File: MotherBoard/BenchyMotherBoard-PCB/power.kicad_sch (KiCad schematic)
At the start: 153 parts, among them J1 PWR-CONN, U1 STM32MP157FAB1, U10 USB7206C, U2 TPS65400RGZT, U3 NCP51200, U4 ATTINY416-MNR, U5 MAX15027, U6 MAX15027, U7 SN74LVC1G32, U8 74HCT2G08, U9 AP2127K-3.3

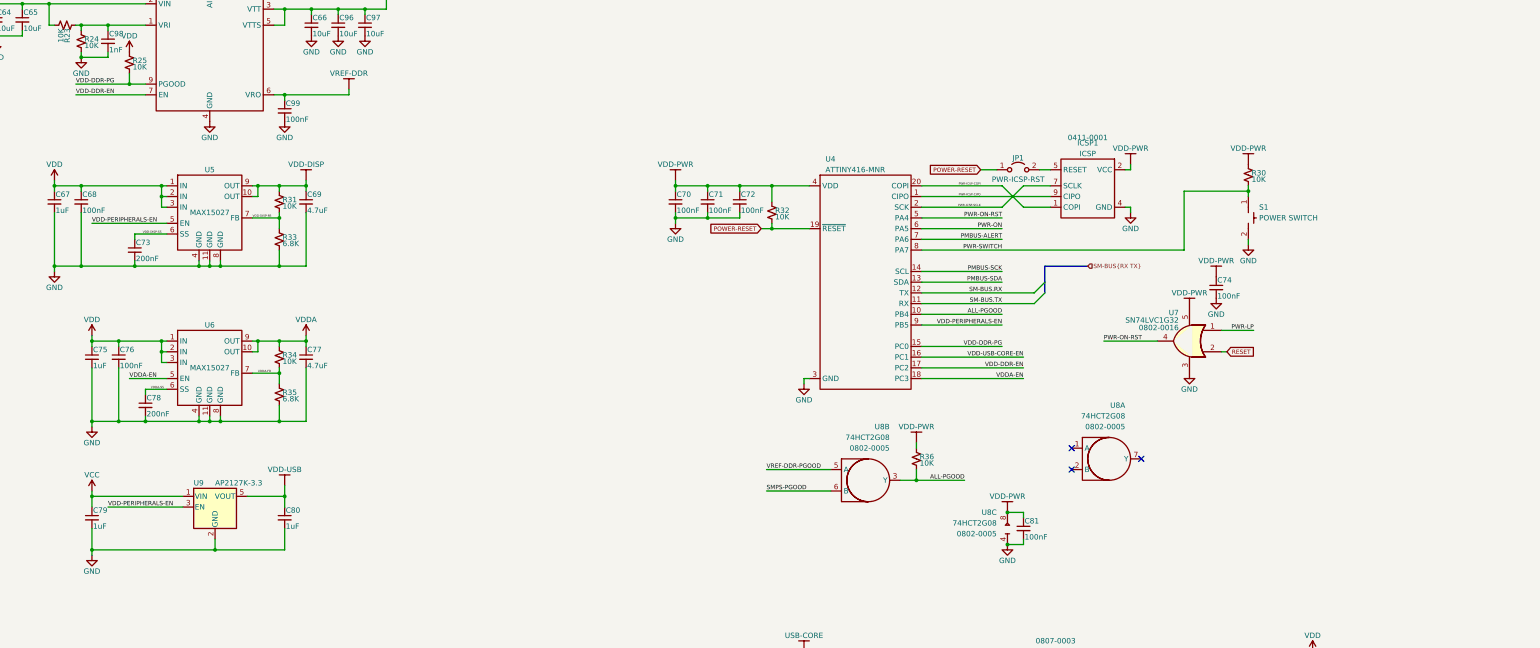
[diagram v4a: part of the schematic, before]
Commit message: Add PGOOD led and replace PWR switch
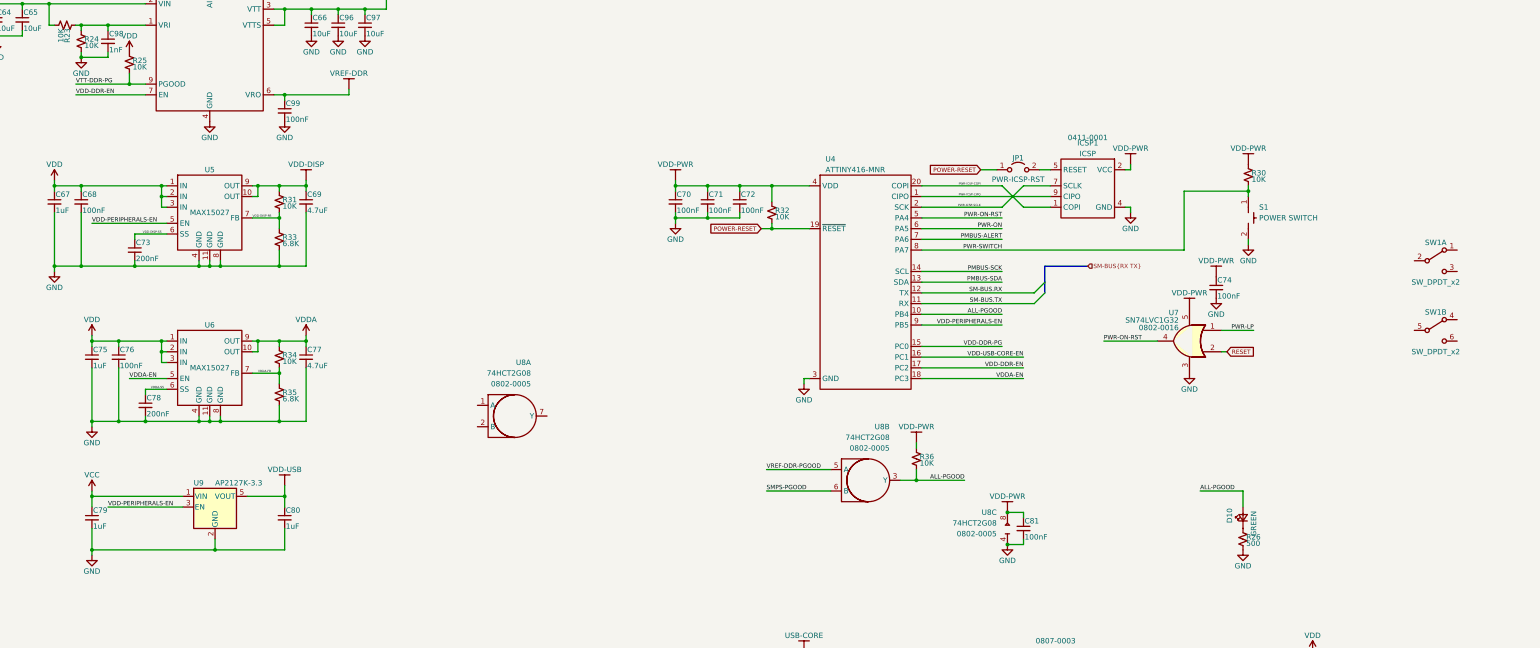
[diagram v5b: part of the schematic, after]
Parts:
- added D10: GREEN, LED_SMD:LED_0805_2012Metric, symbol Device:LED_Small
- added R26: 500, Resistor_SMD:R_0603_1608Metric, symbol Device:R_Small_US
- added SW1: SW_DPDT_x2, Daxxn_Switches:PHAP4383V, symbol Switch:SW_DPDT_x2
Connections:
- net ALL-PGOOD: now also D10.2 (A)
- net GND: now also R26.2
- net VDD-DDR-PG: no longer R25.2, U3.9 (PGOOD)
- new net: D10.1 (K), R26.1
- new net VTT-DDR-PG: R25.2, U3.9 (PGOOD)
- no-connect marks 3 -> 0
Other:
- moved on the sheet: U8A
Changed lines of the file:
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@@
   (junction (at 72.39 38.1) (diameter 0) (color 0 0 0 0)
   )
-  (no_connect (at 323.85 267.97))
-  (no_connect (at 307.34 270.51))
-  (no_connect (at 307.34 265.43))
   (bus_entry (at 298.45 231.14) (size 2.54 -2.54)
     (stroke (width 0) (type default) (color 0 0 0 0))
@@
     (stroke (width 0) (type default) (color 0 0 0 0))
   )
+  (wire (pts (xy 337.82 275.59) (xy 347.98 275.59))
+    (stroke (width 0) (type default) (color 0 0 0 0))
+  )
   (wire (pts (xy 90.17 128.27) (xy 90.17 129.54))
     (stroke (width 0) (type default) (color 0 0 0 0))
@@
     (stroke (width 0) (type default) (color 0 0 0 0))
   )
+  (wire (pts (xy 347.98 279.4) (xy 347.98 275.59))
+    (stroke (width 0) (type default) (color 0 0 0 0))
+  )
   (wire (pts (xy 129.54 74.93) (xy 130.81 74.93))
     (stroke (width 0) (type default) (color 0 0 0 0))
@@
     (effects (font (size 1.016 1.016)) (justify left bottom))
   )
+  (label "ALL-PGOOD" (at 337.82 275.59 0)
+    (effects (font (size 1.016 1.016)) (justify left bottom))
+  )
   (label "VDDA-EN" (at 83.82 248.92 0)
     (effects (font (size 1.016 1.016)) (justify left bottom))
@@
     (effects (font (size 0.5 0.5)) (justify left bottom))
   )
-  (label "VDD-DDR-PG" (at 71.12 179.07 0)
+  (label "VTT-DDR-PG" (at 71.12 179.07 0)
     (effects (font (size 1.016 1.016)) (justify left bottom))
   )
@@
     (pin "1")
   )
+  (symbol (lib_id "Switch:SW_DPDT_x2") (at 393.7 220.98 0) (unit 1)
+    (in_bom yes) (on_board yes)
+    (property "Reference" "SW1" (id 0) (at 393.7 216.662 0))
+    (property "Value" "SW_DPDT_x2" (id 1) (at 393.7 226.06 0))
+    (property "Footprint" "Daxxn_Switches:PHAP4383V" (id 2) (at 393.7 220.98 0)
+      (effects (font (size 1.27 1.27)) hide)
+    )
+    (property "Datasheet" "https://www.mouser.com/datasheet/2/26/appm_s_a0001220312_1-2262200.pdf" (id 3) (at 393.7 220.98 0)
+      (effects (font (size 1.27 1.27)) hide)
+    )
+    (pin "1")
+    (pin "2")
+    (pin "3")
+    (pin "4")
+    (pin "5")
+    (pin "6")
+  )
   (symbol (lib_id "Daxxn_Power:VDD-CORE") (at 264.16 82.55 0) (unit 1)
     (in_bom no) (on_board no)
@@
     (pin "1")
   )
+  (symbol (lib_id "Device:R_Small_US") (at 347.98 287.02 0) (unit 1)
+    (in_bom yes) (on_board yes)
+    (property "Reference" "R26" (id 0) (at 348.742 286.512 0)
+      (effects (font (size 1.27 1.27)) (justify left))
+    )
+    (property "Value" "500" (id 1) (at 348.742 288.036 0)
+      (effects (font (size 1.27 1.27)) (justify left))
+    )
+    (property "Footprint" "Resistor_SMD:R_0603_1608Metric" (id 2) (at 347.98 287.02 0)
+      (effects (font (size 1.27 1.27)) hide)
+    )
+    (property "Datasheet" "~" (id 3) (at 347.98 287.02 0)
+      (effects (font (size 1.27 1.27)) hide)
+    )
+    (pin "1")
+    (pin "2")
+  )
   (symbol (lib_id "Device:R_Small_US") (at 119.38 252.73 0) (unit 1)
     (in_bom yes) (on_board yes)
@@
     (pin "1")
   )
+  (symbol (lib_id "Device:LED_Small") (at 347.98 281.94 90) (unit 1)
+    (in_bom yes) (on_board yes)
+    (property "Reference" "D10" (id 0) (at 344.805 283.21 0)
+      (effects (font (size 1.27 1.27)) (justify left))
+    )
+    (property "Value" "GREEN" (id 1) (at 350.52 286.385 0)
+      (effects (font (size 1.27 1.27)) (justify left))
+    )
+    (property "Footprint" "LED_SMD:LED_0805_2012Metric" (id 2) (at 347.98 281.94 90)
+      (effects (font (size 1.27 1.27)) hide)
+    )
+    (property "Datasheet" "~" (id 3) (at 347.98 281.94 90)
+      (effects (font (size 1.27 1.27)) hide)
+    )
+    (pin "1")
+    (pin "2")
+  )
   (symbol (lib_id "Device:C_Small") (at 72.39 207.01 0) (unit 1)
     (in_bom yes) (on_board yes)
@@
     (pin "2")
   )
+  (symbol (lib_id "Switch:SW_DPDT_x2") (at 393.7 237.49 0) (unit 2)
+    (in_bom yes) (on_board yes)
+    (property "Reference" "SW1" (id 0) (at 393.7 233.172 0))
+    (property "Value" "SW_DPDT_x2" (id 1) (at 393.7 242.57 0))
+    (property "Footprint" "Daxxn_Switches:PHAP4383V" (id 2) (at 393.7 237.49 0)
+      (effects (font (size 1.27 1.27)) hide)
+    )
+    (property "Datasheet" "~" (id 3) (at 393.7 237.49 0)
+      (effects (font (size 1.27 1.27)) hide)
+    )
+    (pin "1")
+    (pin "2")
+    (pin "3")
+    (pin "4")
+    (pin "5")
+    (pin "6")
+  )
   (symbol (lib_id "power:GND") (at 74.93 260.35 0) (unit 1)
     (in_bom yes) (on_board yes)
@@
     (pin "2")
   )
-  (symbol (lib_id "Daxxn_Logic:74HCT2G08") (at 314.96 267.97 0) (unit 1)
+  (symbol (lib_id "Daxxn_Logic:74HCT2G08") (at 173.99 257.81 0) (unit 1)
     (in_bom yes) (on_board yes)
-    (property "Reference" "U8" (id 0) (at 320.04 255.27 0)
+    (property "Reference" "U8" (id 0) (at 179.07 245.11 0)
       (effects (font (size 1.27 1.27)) (justify right))
     )
-    (property "Value" "74HCT2G08" (id 1) (at 320.04 257.81 0)
+    (property "Value" "74HCT2G08" (id 1) (at 179.07 247.65 0)
       (effects (font (size 1.27 1.27)) (justify right))
     )
-    (property "Footprint" "Package_SO:TSSOP-8_3x3mm_P0.65mm" (id 2) (at 314.96 247.65 0)
+    (property "Footprint" "Package_SO:TSSOP-8_3x3mm_P0.65mm" (id 2) (at 173.99 237.49 0)
       (effects (font (size 1.27 1.27)) hide)
     )
-    (property "Datasheet" "%LOCAL_DATASHEETS%\\74HC2G08.pdf" (id 3) (at 314.96 245.11 0)
+    (property "Datasheet" "%LOCAL_DATASHEETS%\\74HC2G08.pdf" (id 3) (at 173.99 234.95 0)
       (effects (font (size 1.27 1.27)) hide)
     )
-    (property "PartNumber" "0802-0005" (id 4) (at 320.04 260.35 0)
+    (property "PartNumber" "0802-0005" (id 4) (at 179.07 250.19 0)
       (effects (font (size 1.27 1.27)) (justify right))
     )
@@
     (pin "2")
   )
+  (symbol (lib_id "power:GND") (at 347.98 289.56 0) (unit 1)
+    (in_bom yes) (on_board yes)
+    (property "Reference" "#PWR0218" (id 0) (at 347.98 295.91 0)
+      (effects (font (size 1.27 1.27)) hide)
+    )
+    (property "Value" "GND" (id 1) (at 347.98 293.37 0))
+    (property "Footprint" "" (id 2) (at 347.98 289.56 0)
+      (effects (font (size 1.27 1.27)) hide)
+    )
+    (property "Datasheet" "" (id 3) (at 347.98 289.56 0)
+      (effects (font (size 1.27 1.27)) hide)
+    )
+    (pin "1")
+  )
   (symbol (lib_id "Device:C_Small") (at 300.99 34.29 0) (unit 1)

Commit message: Start DDR3 layout
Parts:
- removed R36: 10K, Resistor_SMD:R_0402_1005Metric, symbol Device:R_Small_US
- removed S1: POWER SWITCH, Daxxn_Switches:TL3365AF180QG, symbol Daxxn_Buttons:GENERIC-SWITCH-2P
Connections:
- net GND: now also SW1.3 (C)
- net PWR-SWITCH: now also SW1.2 (B)
- no-connect marks 0 -> 1
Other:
- note removed: "COMP NOT CALCULATED YET"
- moved on the sheet: R30, SW1A, SW1B, U8A

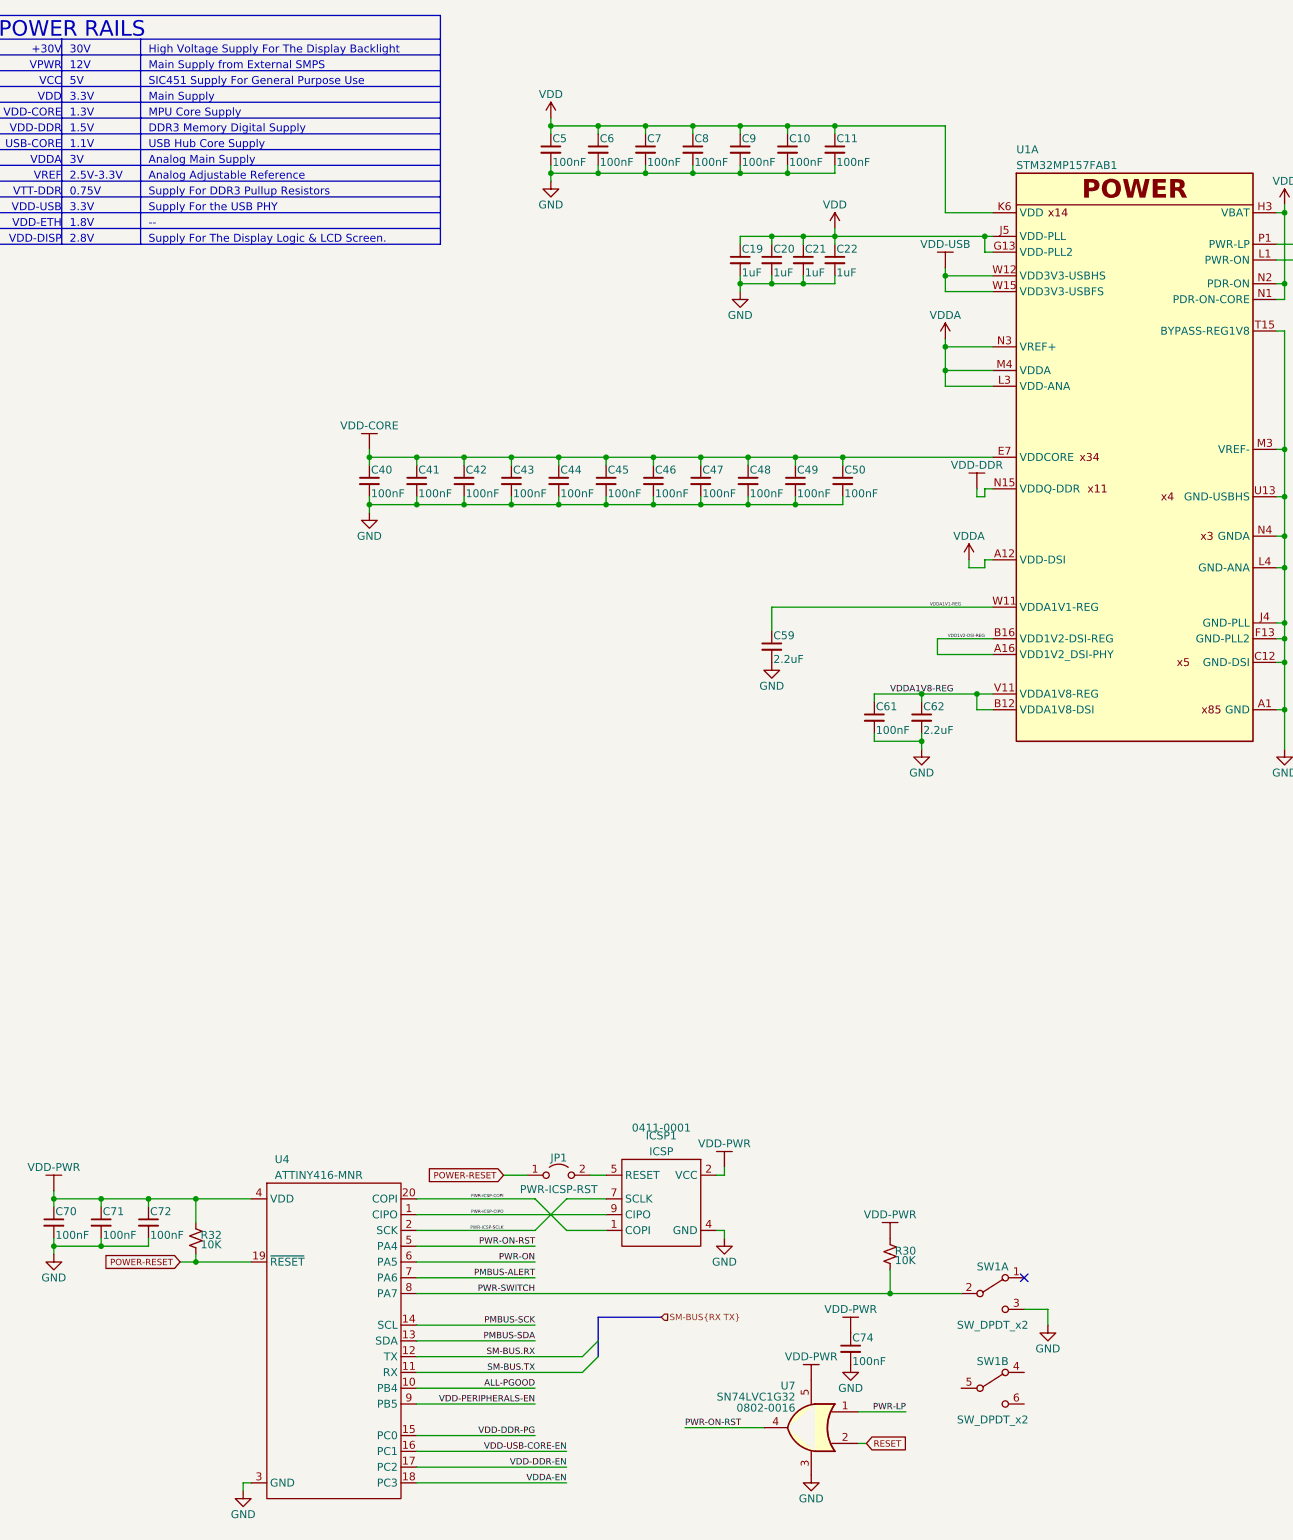
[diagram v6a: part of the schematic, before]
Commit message: Finish DDR3 memory layout
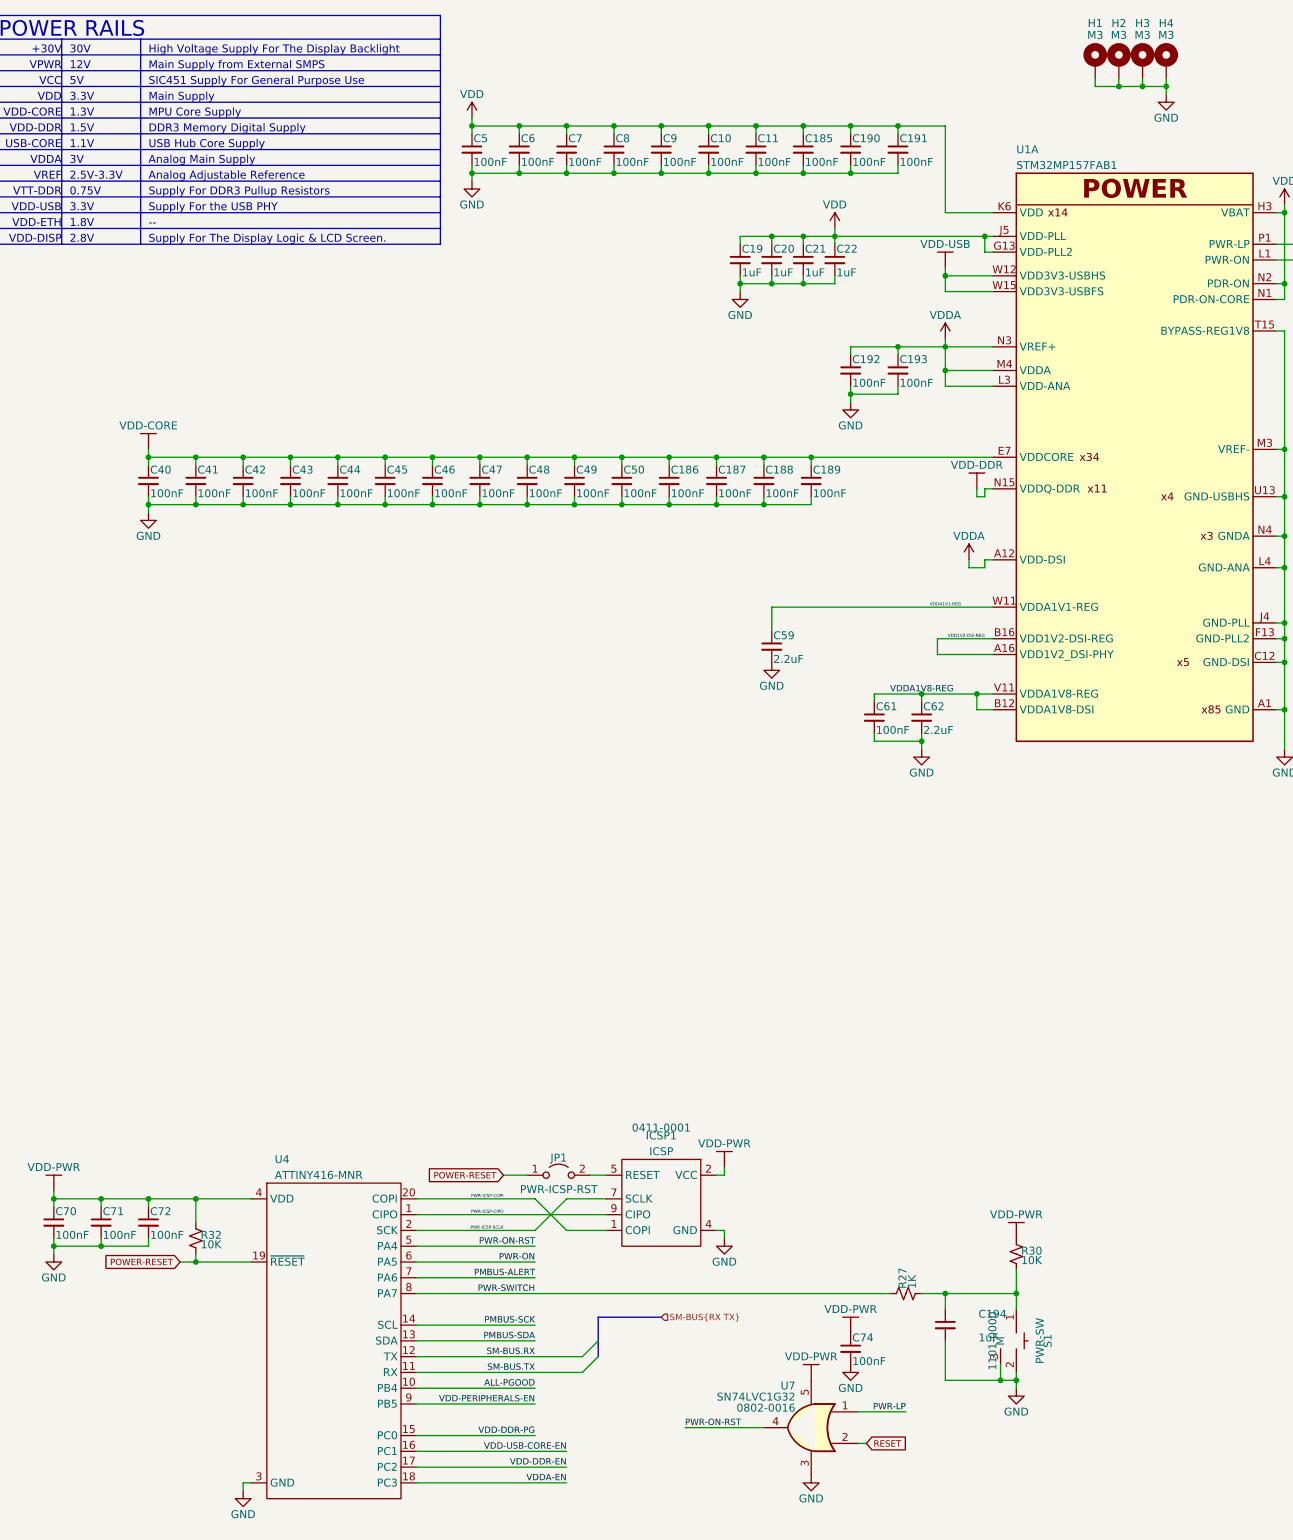
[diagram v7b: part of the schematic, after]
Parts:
- removed SW1: SW_DPDT_x2, Daxxn_Switches:PHAP4383V, symbol Switch:SW_DPDT_x2
- added C185, C186, C187, C188, C189, C190, C191, C192, C193: 100nF, Capacitor_SMD:C_0402_1005Metric, symbol Device:C_Small
- added C194: 1uF, Capacitor_SMD:C_0603_1608Metric, symbol Device:C_Small
- added H1, H2, H3, H4: M3, MountingHole:MountingHole_3.5mm_Pad_Via, symbol Mechanical:MountingHole_Pad
- added R27: 1K, Resistor_SMD:R_0402_1005Metric, symbol Device:R_Small_US
- added S1: PWR-SW, Daxxn_Switches:TL1105SF, symbol Daxxn_Buttons:GENERIC-SWITCH-2P-M
- U3: footprint Package_DFN_QFN:DFN-10-1EP_3x3mm_P0.5mm_EP1.7x2.5mm -> Daxxn_Packages:DFN-10-1EP_3x3mm_P0.5mm_EP1.65x2.38mm
- U4: footprint Package_DFN_QFN:VQFN-20-1EP_3x3mm_P0.4mm_EP1.7x1.7mm -> Daxxn_Packages:QFN-20-1EP_3x3mm_P0.4mm_EP1.65x1.65mm
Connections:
- net GND: now also C185.2, C186.2, C187.2, C188.2, C189.2, C190.2, C191.2, C192.2, C193.2, C194.2, H1.1, H2.1, H3.1, H4.1, S1.2, S1.3 (M)
- net PWR-SWITCH: now also R27.1; no longer R30.2
- net VDD: now also C185.1, C190.1, C191.1
- net VDD-CORE: now also C186.1, C187.1, C188.1, C189.1
- net VDDA: now also C192.1, C193.1
- new net: C194.1, R27.2, R30.2, S1.1
- no-connect marks 1 -> 0
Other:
- moved on the sheet: C10, C11, C40, C41, C42, C43, C44, C45, C46, C47, C48, C49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

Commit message: Mostly routed USB
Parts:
- removed C69: 4.7uF, Capacitor_SMD:C_0603_1608Metric, symbol Device:C_Small
- removed C70: 100nF, Capacitor_SMD:C_0402_1005Metric, symbol Device:C_Small
- removed C73: 200nF, Capacitor_SMD:C_0402_1005Metric, symbol Device:C_Small
- removed R31: 10K, Resistor_SMD:R_0402_1005Metric, symbol Device:R_Small_US
- removed R33: 6.8K, Resistor_SMD:R_0402_1005Metric, symbol Device:R_Small_US
- removed U5: MAX15027, Package_DFN_QFN:DFN-10-1EP_3x3mm_P0.5mm_EP1.65x2.38mm, symbol Daxxn_Regulators:MAX15027
- added H5, H6, H7, H8, H9: M2, MountingHole:MountingHole_2.2mm_M2_ISO7380_Pad, symbol Mechanical:MountingHole_Pad
- C67: value 1uF -> 100nF; footprint Capacitor_SMD:C_0603_1608Metric -> Capacitor_SMD:C_0402_1005Metric
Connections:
- net GND: now also H5.1, H6.1, H7.1, H8.1, H9.1
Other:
- note removed: "--"
- note removed: "1.8V"
- note removed: "2.8V"
- note removed: "Supply For The Display Logic & LCD Screen."
- note removed: "VDD-DISP"
- note removed: "VDD-ETH"
- moved on the sheet: C71, C72, C93, C94, C95
